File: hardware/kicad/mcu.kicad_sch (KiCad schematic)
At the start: 12 parts, among them J601 Pulsanti (contenitore), SW601 MODE, SW602 SET, U601 Raspberry Pi Pico, U602 MB85RC256V (FRAM)

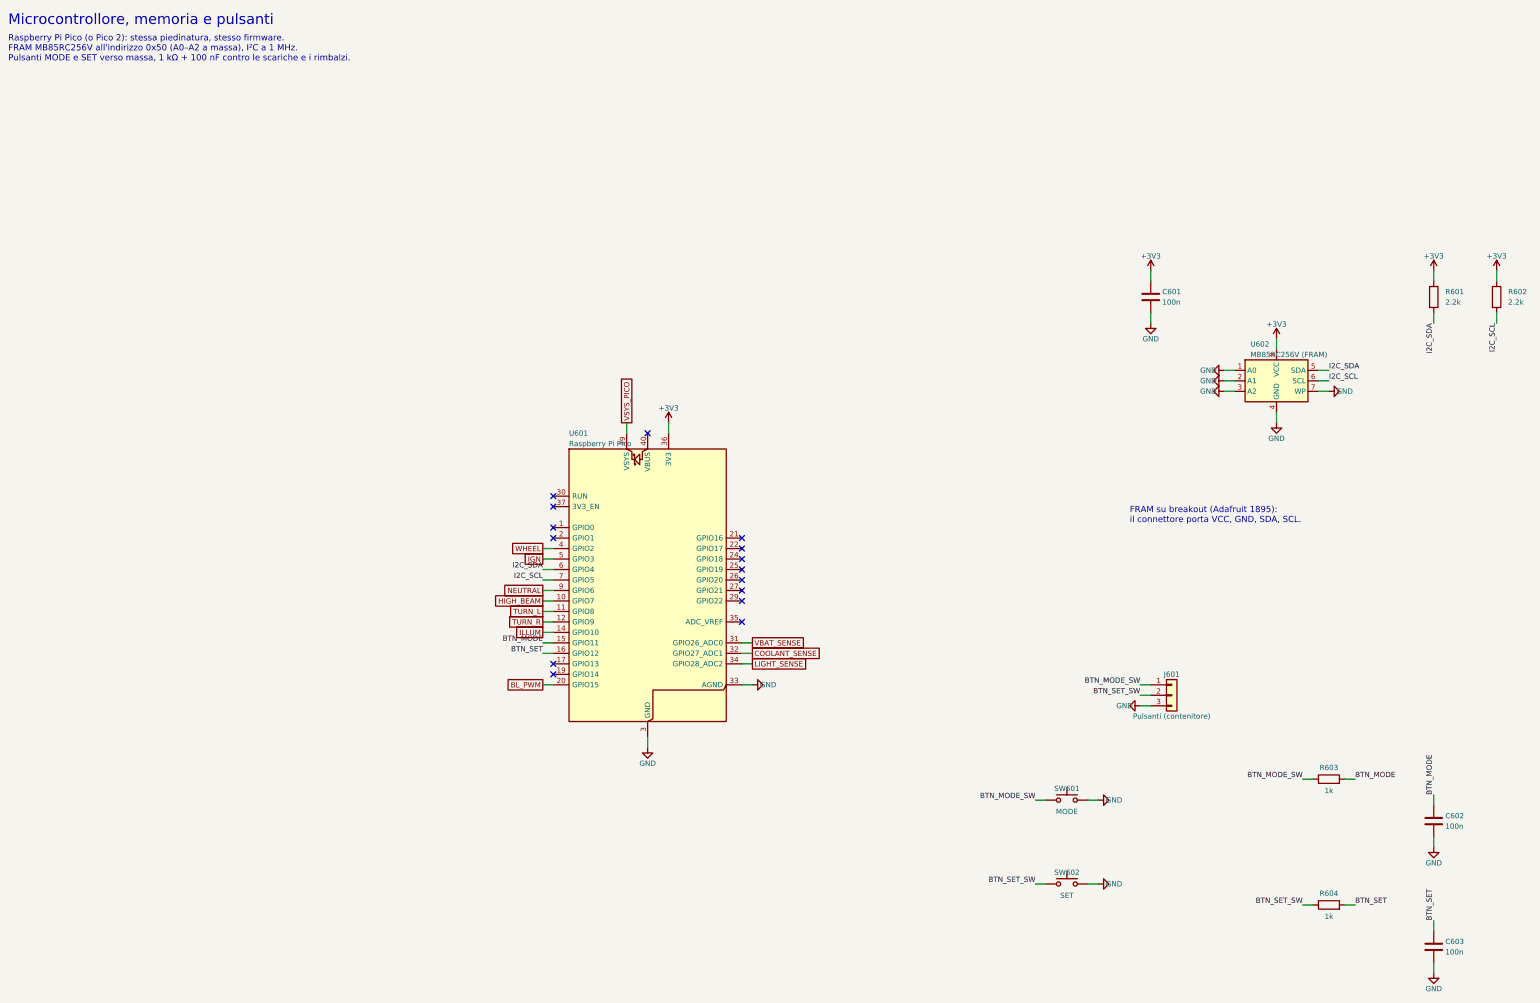
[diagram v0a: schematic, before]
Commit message: Translate code, hardware and docs to English; bilingual dashboard
- tdm-logic i18n module: every dashboard text in English and Italian,
  chosen by `[display] language` in the profile (English by default, the
  TDM 850 profile keeps Italian); number formatting per language
- Slint fixed labels moved to a `Labels` global filled from the same table;
  `tdm-dash --language en|it`; reference screens regenerated in English with
  Italian check screens
- tdmctl, tdm-dash CLI, simulator scenarios, calibration errors and tools
  print English
- KiCad sheets, WireViz harnesses, perfboard plan and CAD comments in
  English, exports regenerated with the new names
- manual, research, ADRs and READMEs translated; files renamed (docs/manual,
  docs/research, English chapter and ADR names); status markers are now
  [VERIFIED] / [TO VERIFY] / [HYPOTHESIS]

Co-Authored-By: Claude Opus 5.5 <noreply@anthropic.com>
Claude-Session: https://claude.ai/code/session_01G9D4Wshjz9MkaThp4wsrGP
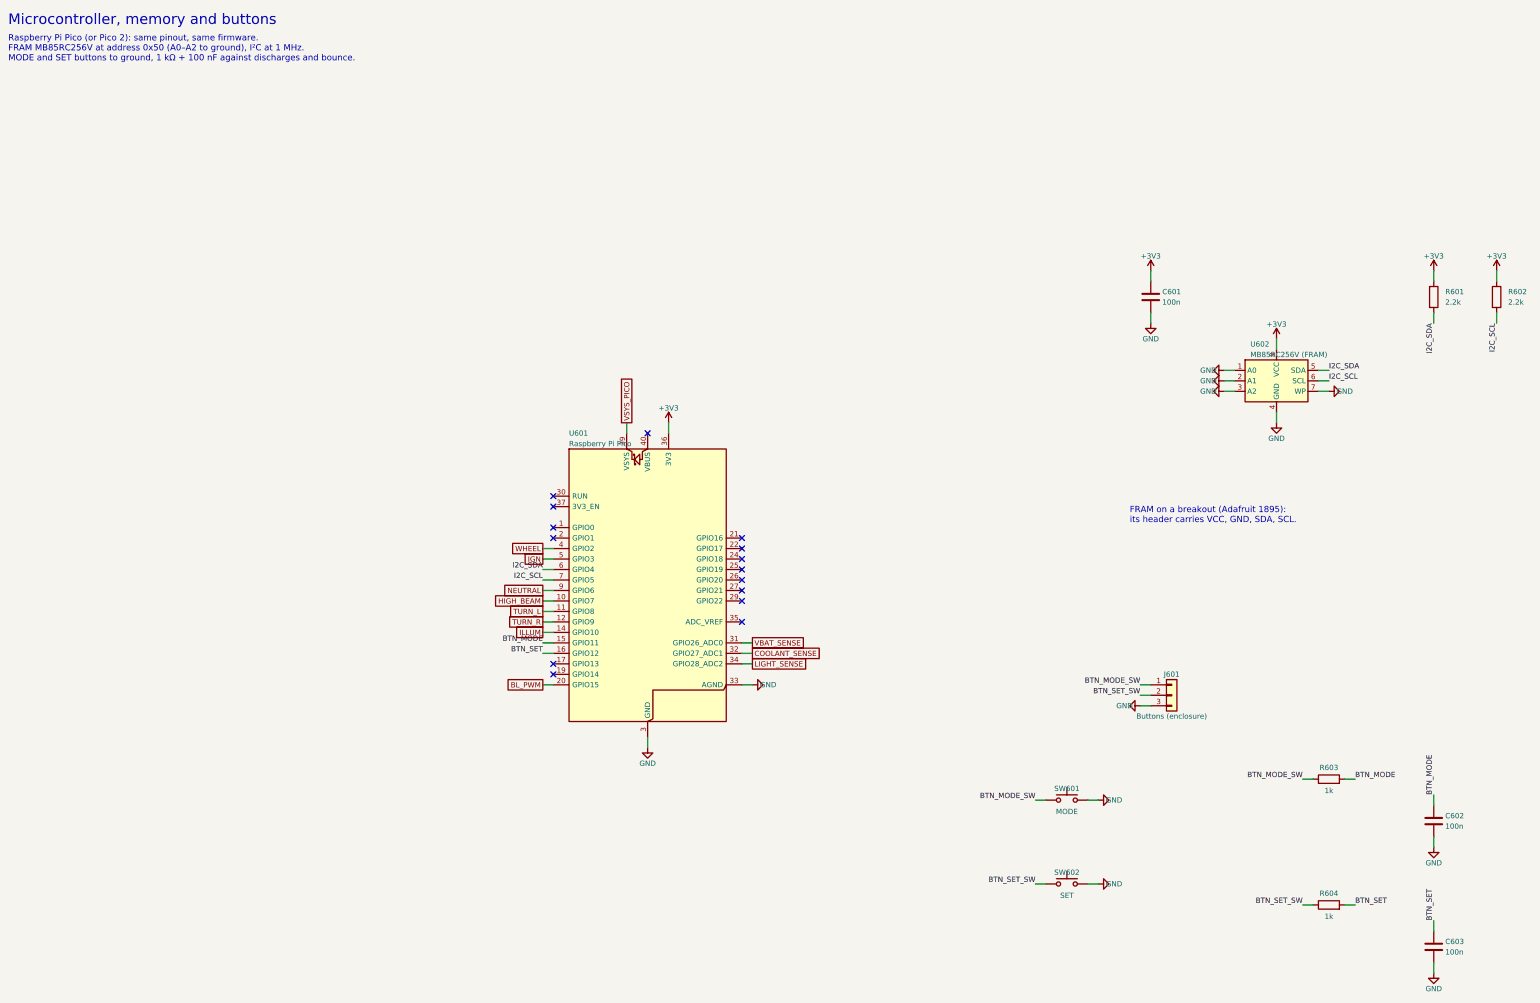
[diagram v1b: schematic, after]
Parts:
- J601: value Pulsanti (contenitore) -> Buttons (enclosure)
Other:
- note added: "FRAM on a breakout (Adafruit 1895): its header carries VCC, GND, SDA, SCL."
- note added: "Microcontroller, memory and buttons"
- note added: "Raspberry Pi Pico (or Pico 2): same pinout, same firmware. FRAM MB85RC256V at address 0x50 (A0–A2 to ground), I²C at 1 MHz. MODE and SET buttons to ground, 1 kΩ + 100 nF against discharges and bounce."
- note removed: "FRAM su breakout (Adafruit 1895): il connettore porta VCC, GND, SDA, SCL."
- note removed: "Microcontrollore, memoria e pulsanti"
- note removed: "Raspberry Pi Pico (o Pico 2): stessa piedinatura, stesso firmware. FRAM MB85RC256V all'indirizzo 0x50 (A0–A2 a massa), I²C a 1 MHz. Pulsanti MODE e SET verso massa, 1 kΩ + 100 nF contro le scariche e i rimbalzi."
- title: Pico, FRAM e pulsanti -> Pico, FRAM and buttons
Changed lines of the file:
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@@
 	(paper "A3")
 	(title_block
-		(title "Pico, FRAM e pulsanti")
+		(title "Pico, FRAM and buttons")
 		(date "2026-10-21")
 		(rev "0.1")
 		(company "tdm-dash · CERN-OHL-P-2.0")
-		(comment 1 "Foglio 6 di 8")
-		(comment 2 "Generato da hardware/kicad/generate.py: non modificare a mano")
+		(comment 1 "Sheet 6 of 8")
+		(comment 2 "Generated by hardware/kicad/generate.py: do not edit by hand")
 	)
 	(symbol
@@
 			)
 		)
-		(property "Value" "Pulsanti (contenitore)"
+		(property "Value" "Buttons (enclosure)"
 			(at 292.1 182.88 0)
 			(effects
@@
 		)
 	)
-	(text "Microcontrollore, memoria e pulsanti"
+	(text "Microcontroller, memory and buttons"
 		(exclude_from_sim no)
 		(at 10.16 12.7 0)
@@
 		)
 	)
-	(text "Raspberry Pi Pico (o Pico 2): stessa piedinatura, stesso firmware.\nFRAM MB85RC256V all'indirizzo 0x50 (A0–A2 a massa), I²C a 1 MHz.\nPulsanti MODE e SET verso massa, 1 kΩ + 100 nF contro le scariche e i rimbalzi."
+	(text "Raspberry Pi Pico (or Pico 2): same pinout, same firmware.\nFRAM MB85RC256V at address 0x50 (A0–A2 to ground), I²C at 1 MHz.\nMODE and SET buttons to ground, 1 kΩ + 100 nF against discharges and bounce."
 		(exclude_from_sim no)
 		(at 10.16 17.78 0)
@@
 		)
 	)
-	(text "FRAM su breakout (Adafruit 1895):\nil connettore porta VCC, GND, SDA, SCL."
+	(text "FRAM on a breakout (Adafruit 1895):\nits header carries VCC, GND, SDA, SCL."
 		(exclude_from_sim no)
 		(at 281.94 132.08 0)

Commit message: Schematic: drawn wires, block diagram, new title block
The sheets were a netlist in disguise: every pin ended in a short stub and
a label, so the circuits had to be pieced together by name, labels
overlapped, two sheets fell off the index page and the title block was
KiCad's default. The generator now draws the schematic:

- hardware/kicad/schgen: placement on the 50 mil grid, orthogonal wires,
  junctions, hierarchical ports, module and connector symbols with named
  pins; the drawing is normalised the way KiCad 9 reads it and checked
  against the declared netlist (no wire may connect anything else)
- hardware/kicad/sheets: one module per sheet, laid out left to right
  from the bike to the Pico; the root sheet is a block diagram whose
  wires are the signals between sheets
- tdm-dash.kicad_wks: frame and title block of the project
- symbols copied from KiCad 9.0.9 (vendor_symbols.py): the generator no
  longer needs KiCad installed
- export.sh: ERC, tools/check_netlist.py (KiCad's netlist is the declared
  one), check_pinmap.py, PDF and SVG on white, tools/check_svg_layout.py
  (no text over another text, a wire, the frame or the title block)

The circuit is unchanged: KiCad's netlist of the old and new schematic
has the same 56 nets (FRAM pins now follow the breakout header, R603/R604
pins swapped).

Co-Authored-By: Claude Opus 5.5 <noreply@anthropic.com>
Claude-Session: https://claude.ai/code/session_01G9D4Wshjz9MkaThp4wsrGP
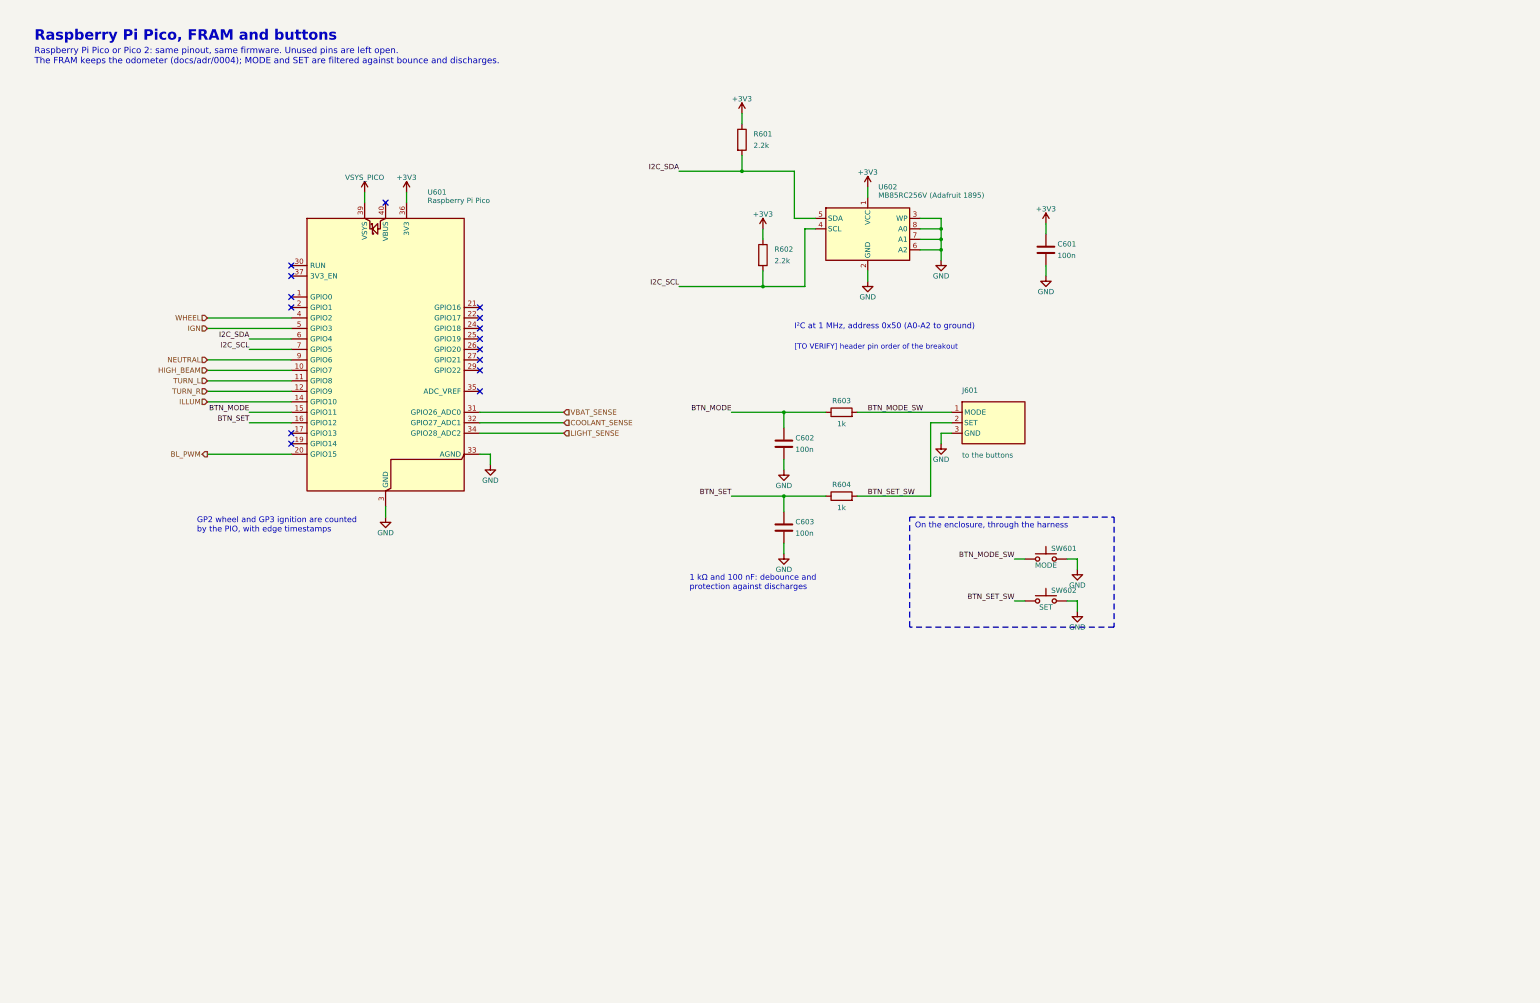
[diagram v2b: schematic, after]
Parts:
- removed J601: Buttons (enclosure), symbol Connector_Generic:Conn_01x03
- removed U602: MB85RC256V (FRAM), symbol Memory_EEPROM:24LC256
- added J601: to the buttons, symbol tdm:Conn_Buttons3
- added U602: MB85RC256V (Adafruit 1895), symbol tdm:FRAM_Breakout
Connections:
- net +3V3: now also U602.1 (VCC)
- net BTN_MODE: now also R603.1; no longer R603.2
- net BTN_MODE_SW: now also R603.2, J601.1 (MODE); no longer R603.1
- net BTN_SET: now also R604.1; no longer R604.2
- net BTN_SET_SW: now also R604.2, J601.2 (SET); no longer R604.1
- net GND: now also J601.3 (GND), U602.2 (GND), U602.3 (WP), U602.6 (A2), U602.7 (A1), U602.8 (A0)
- net I2C_SCL: now also U602.4 (SCL)
- net I2C_SDA: now also U602.5 (SDA)
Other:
- note added: "1 kΩ and 100 nF: debounce and protection against discharges"
- note added: "GP2 wheel and GP3 ignition are counted by the PIO, with edge timestamps"
- note added: "I²C at 1 MHz, address 0x50 (A0-A2 to ground)"
- note added: "On the enclosure, through the harness"
- note added: "Raspberry Pi Pico or Pico 2: same pinout, same firmware. Unused pins are left open. The FRAM keeps the odometer (docs/adr/0004); MODE and SET are filtered against bounce and discharges."
- note added: "Raspberry Pi Pico, FRAM and buttons"
- note added: "[TO VERIFY] header pin order of the breakout"
- note removed: "FRAM on a breakout (Adafruit 1895): its header carries VCC, GND, SDA, SCL."
- note removed: "Microcontroller, memory and buttons"
- note removed: "Raspberry Pi Pico (or Pico 2): same pinout, same firmware. FRAM MB85RC256V at address 0x50 (A0–A2 to ground), I²C at 1 MHz. MODE and SET buttons to ground, 1 kΩ + 100 nF against discharges and bounce."
- company: tdm-dash · CERN-OHL-P-2.0 -> tdm-dash
